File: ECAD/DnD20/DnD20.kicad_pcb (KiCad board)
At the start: 2 copper layers, 55 x 89 mm, 38 parts, among them IC1g$1 CP2104, J1 Conn_01x03_Female, J2 Conn_01x04_Female, Q1 2N2219, Q2 2N2219, SW1 switch, SW2 switch, U1 ESP12, U2 AP2112-3.3, U3 MCP73831/2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

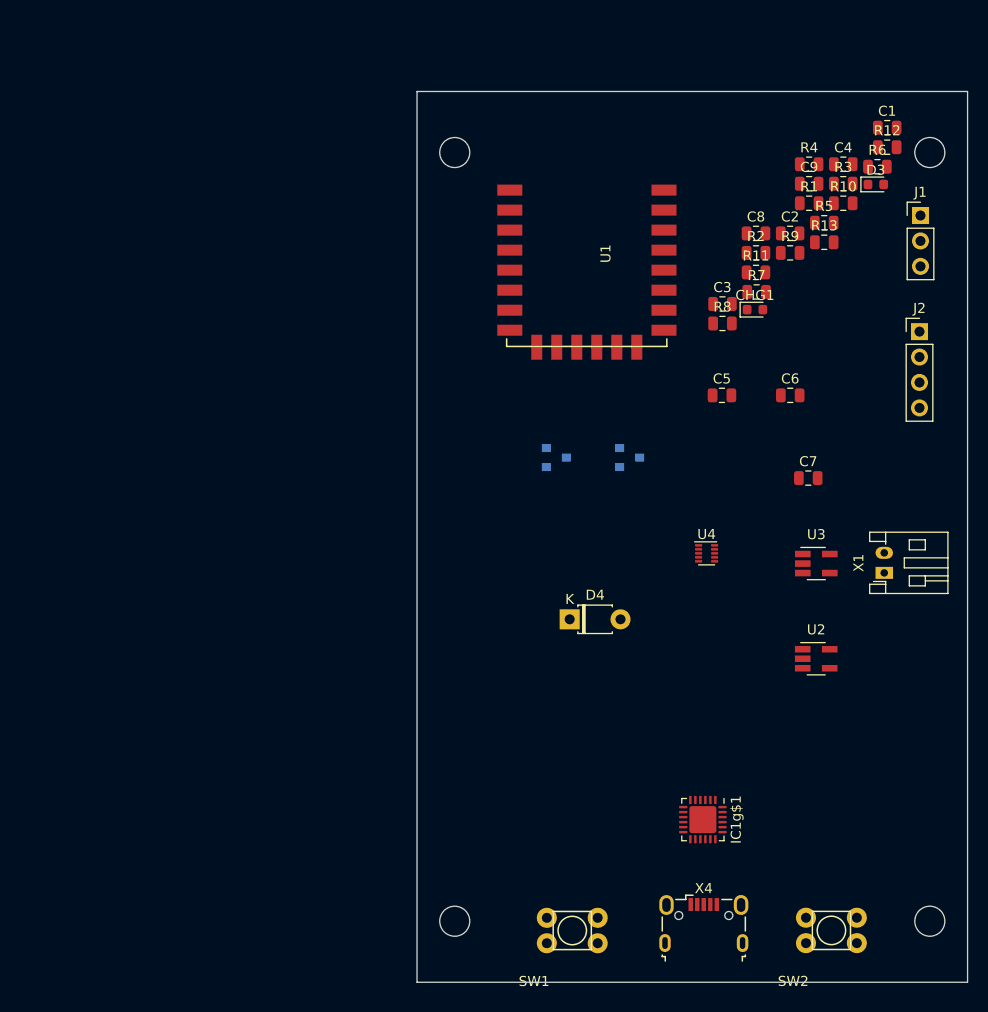
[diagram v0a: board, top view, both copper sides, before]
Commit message: Refactored firmware before removing accelerometer
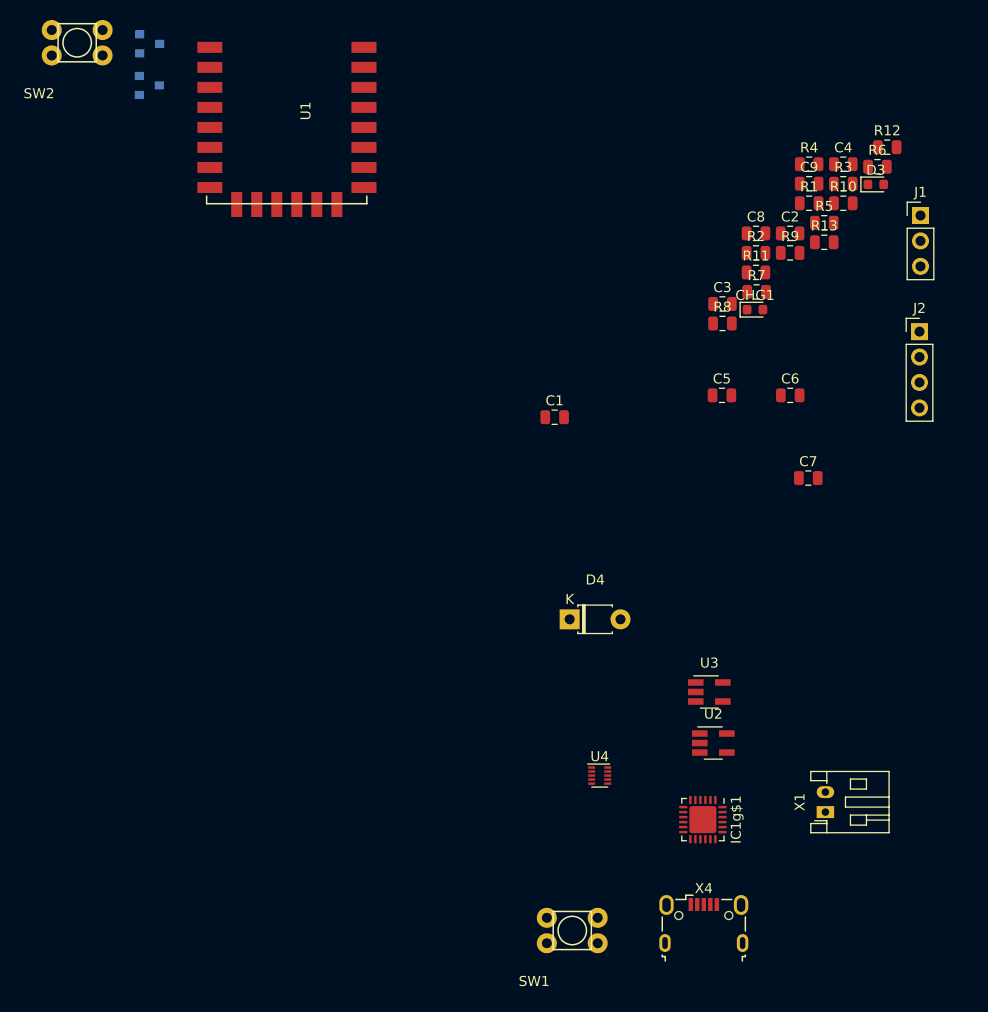
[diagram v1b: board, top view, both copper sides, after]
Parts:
- moved SW2 116.4 mm to (87.0, 59.5)
- moved Q2 63.3 mm to (94.3, 55.8)
- moved Q1 55.1 mm to (94.2, 59.9)
- moved C1 44.1 mm to (134.8, 93.0)
- moved U1 33.2 mm to (101.0, 56.1)
- moved U4 24.6 mm to (139.2, 128.8)
- moved X1 24.6 mm to (161.8, 132.5)
- moved U3 16.7 mm to (150.2, 120.5)
- moved U2 13.3 mm to (150.6, 125.6)
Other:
- board outline removed
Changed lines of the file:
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@@
-(kicad_pcb (version 20171130) (host pcbnew 5.0.0-fee4fd1~66~ubuntu18.04.1)
+(kicad_pcb (version 20171130) (host pcbnew "(5.0.1)-4")
   (general
     (thickness 1.6)
-    (drawings 8)
+    (drawings 0)
     (tracks 0)
     (zones 0)
@@
     (pad_drill 0.762)
     (pad_to_mask_clearance 0.2)
+    (solder_mask_min_width 0.25)
     (aux_axis_origin 0 0)
-    (visible_elements FFFFF77F)
+    (visible_elements 7FFFF7FF)
     (pcbplotparams
       (layerselection 0x00030_80000001)
@@
   )
   (module Package_TO_SOT_SMD:SOT-23 (layer B.Cu)
-    (at 142.24 97.08)
+    (at 94.3 55.75)
     (descr "SOT-23, Standard")
     (tags SOT-23)
@@
       (effects (font (size 1 1) (thickness 0.15)) (justify mirror))
     )
-    (fp_text value 2N2219 (at 0 -2.5) (layer B.Fab)
+    (fp_text value 2N2219 (at 5.7 -2.2) (layer B.Fab)
       (effects (font (size 1 1) (thickness 0.15)) (justify mirror))
     )
@@
   )
   (module Package_TO_SOT_SMD:SOT-23 (layer B.Cu)
-    (at 134.92 97.08)
+    (at 94.25 59.9)
     (descr "SOT-23, Standard")
     (tags SOT-23)
@@
   )
   (module Capacitor_SMD:C_0805_2012Metric (layer F.Cu)
-    (at 167.975001 64.125001)
+    (at 134.75 93.05)
     (descr "Capacitor SMD 0805 (2012 Metric), square (rectangular) end terminal, IPC_7351 nominal, (Body size source: https://docs.google.com/spreadsheets/d/1BsfQQcO9C6DZCsRaXUlFlo91Tg2WpOkGARC1WS5S8t0/edit?usp=sharing), generated with kicad-footprint-generator")
     (tags capacitor)
@@
     (descr "Diode, T-1 series, Axial, Horizontal, pin pitch=5.08mm, , length*diameter=3.2*2.6mm^2, , http://www.diodes.com/_files/packages/T-1.pdf")
     (tags "Diode T-1 series Axial Horizontal pin pitch 5.08mm  length 3.2mm diameter 2.6mm")
-    (fp_text reference D4 (at 2.54 -2.42) (layer F.SilkS)
+    (fp_text reference D4 (at 2.55 -3.94) (layer F.SilkS)
       (effects (font (size 1 1) (thickness 0.15)))
     )
@@
   )
   (module Button_Switch_THT:clicky_button (layer F.Cu)
-    (at 162.4 148.13 180)
+    (at 87.05 59.45 180)
     (fp_text reference SW2 (at 3.81 -1.27 180) (layer F.SilkS)
       (effects (font (size 1 1) (thickness 0.15)))
@@
   )
   (module ESP8266:ESP-12E_SMD (layer F.Cu)
-    (at 130.97 70.36)
+    (at 101 56.1)
     (descr "Module, ESP-8266, ESP-12, 16 pad, SMD")
     (tags "Module ESP-8266 ESP8266")
@@
   )
   (module Package_TO_SOT_SMD:SOT-23-5_HandSoldering (layer F.Cu)
-    (at 160.88 117.18)
+    (at 150.6 125.6)
     (descr "5-pin SOT23 package")
     (tags "SOT-23-5 hand-soldering")
@@
   )
   (module Package_TO_SOT_SMD:SOT-23-5_HandSoldering (layer F.Cu)
-    (at 160.89 107.67)
+    (at 150.2 120.5)
     (descr "5-pin SOT23 package")
     (tags "SOT-23-5 hand-soldering")
@@
   )
   (module Package_DFN_QFN:DFN-10_2x2mm_P0.4mm (layer F.Cu)
-    (at 149.93 106.65)
+    (at 139.25 128.85)
     (descr "10-Lead Plastic DFN (2mm x 2mm)  0.40mm pitch")
     (tags "DFN 10 0.4mm")
@@
   )
   (module Connector_JST:JST_PH_S2B-PH-K_1x02_P2.00mm_Horizontal (layer F.Cu)
-    (at 167.68 108.6 90)
+    (at 161.8 132.5 90)
     (descr "JST PH series connector, S2B-PH-K (http://www.jst-mfg.com/product/pdf/eng/ePH.pdf), generated with kicad-footprint-generator")
     (tags "connector JST PH top entry")
@@
     )
   )
-  (gr_circle (center 124.770108 66.606855) (end 126.270108 66.606855) (layer Edge.Cuts) (width 0.1))
-  (gr_circle (center 172.232092 66.606855) (end 173.732092 66.606855) (layer Edge.Cuts) (width 0.1))
-  (gr_circle (center 124.770108 143.400345) (end 126.270108 143.400345) (layer Edge.Cuts) (width 0.1))
-  (gr_circle (center 172.232092 143.400345) (end 173.732092 143.400345) (layer Edge.Cuts) (width 0.1))
-  (gr_line (start 121.0011 149.4986) (end 121.0011 60.5086) (layer Edge.Cuts) (width 0.1))
-  (gr_line (start 176.0011 149.4986) (end 121.0011 149.4986) (layer Edge.Cuts) (width 0.1))
-  (gr_line (start 176.0011 60.5086) (end 176.0011 149.4986) (layer Edge.Cuts) (width 0.1))
-  (gr_line (start 121.0011 60.5086) (end 176.0011 60.5086) (layer Edge.Cuts) (width 0.1))
 )
